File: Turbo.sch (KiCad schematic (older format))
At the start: 25 parts, among them U12 74HCT27, U13 74HCT74, U14 74F86, U15 74F74, U16 74HCT04, U17 74HCT112, U18 74F157, U19 74F157

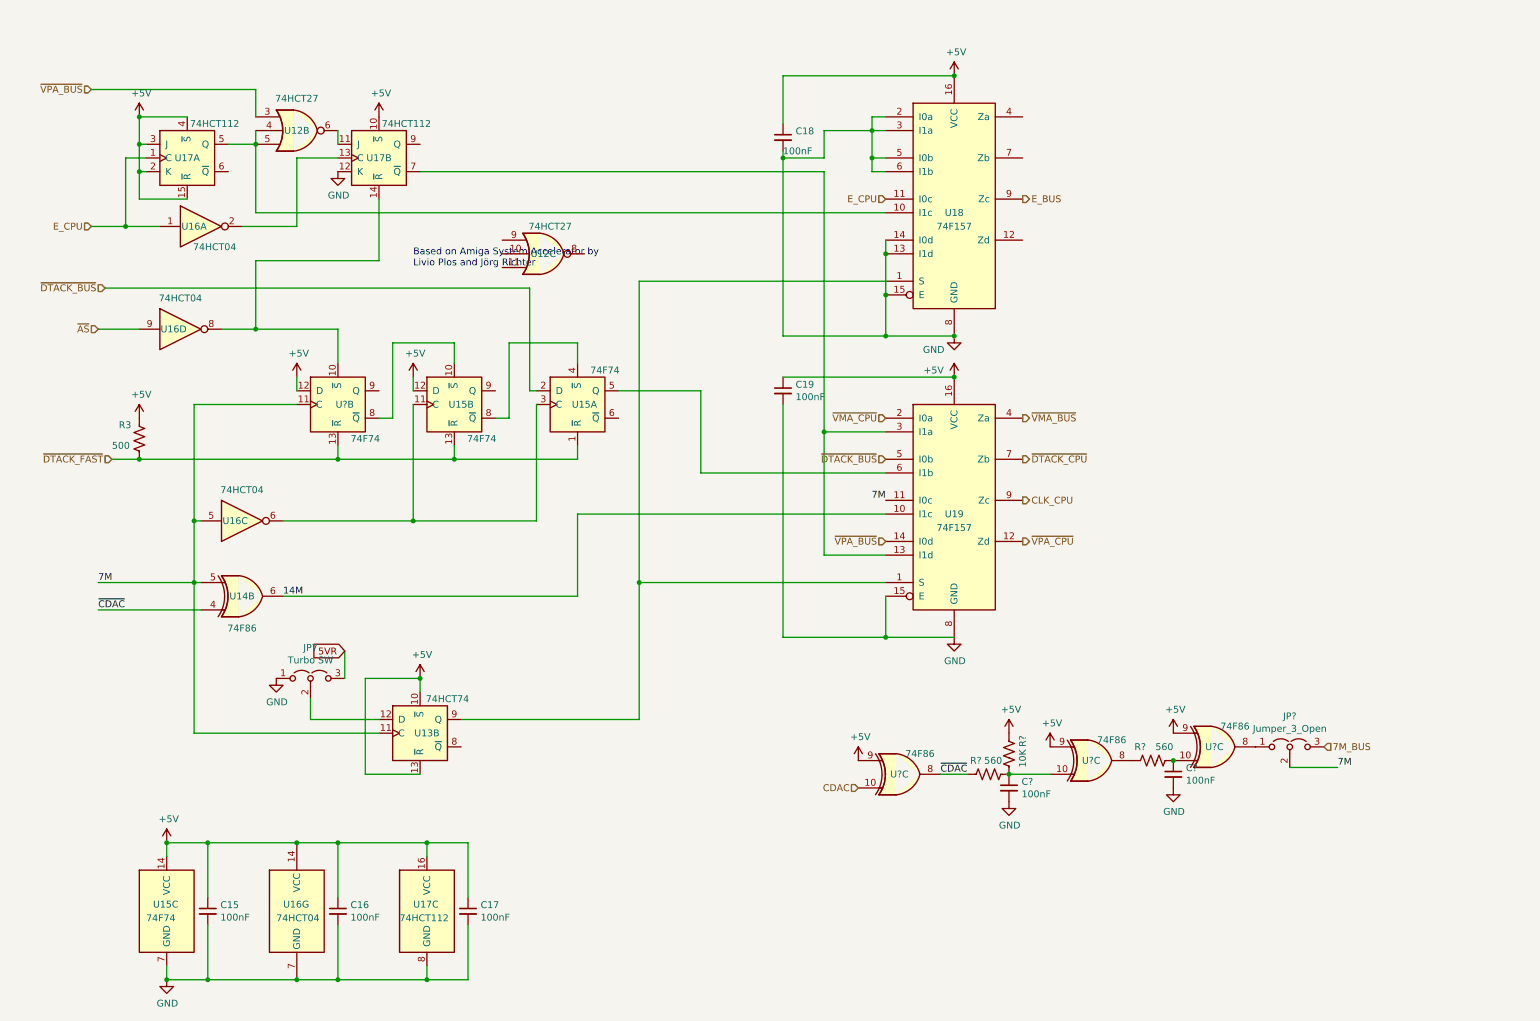
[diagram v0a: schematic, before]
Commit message: AS UDS LDS delay in schematics
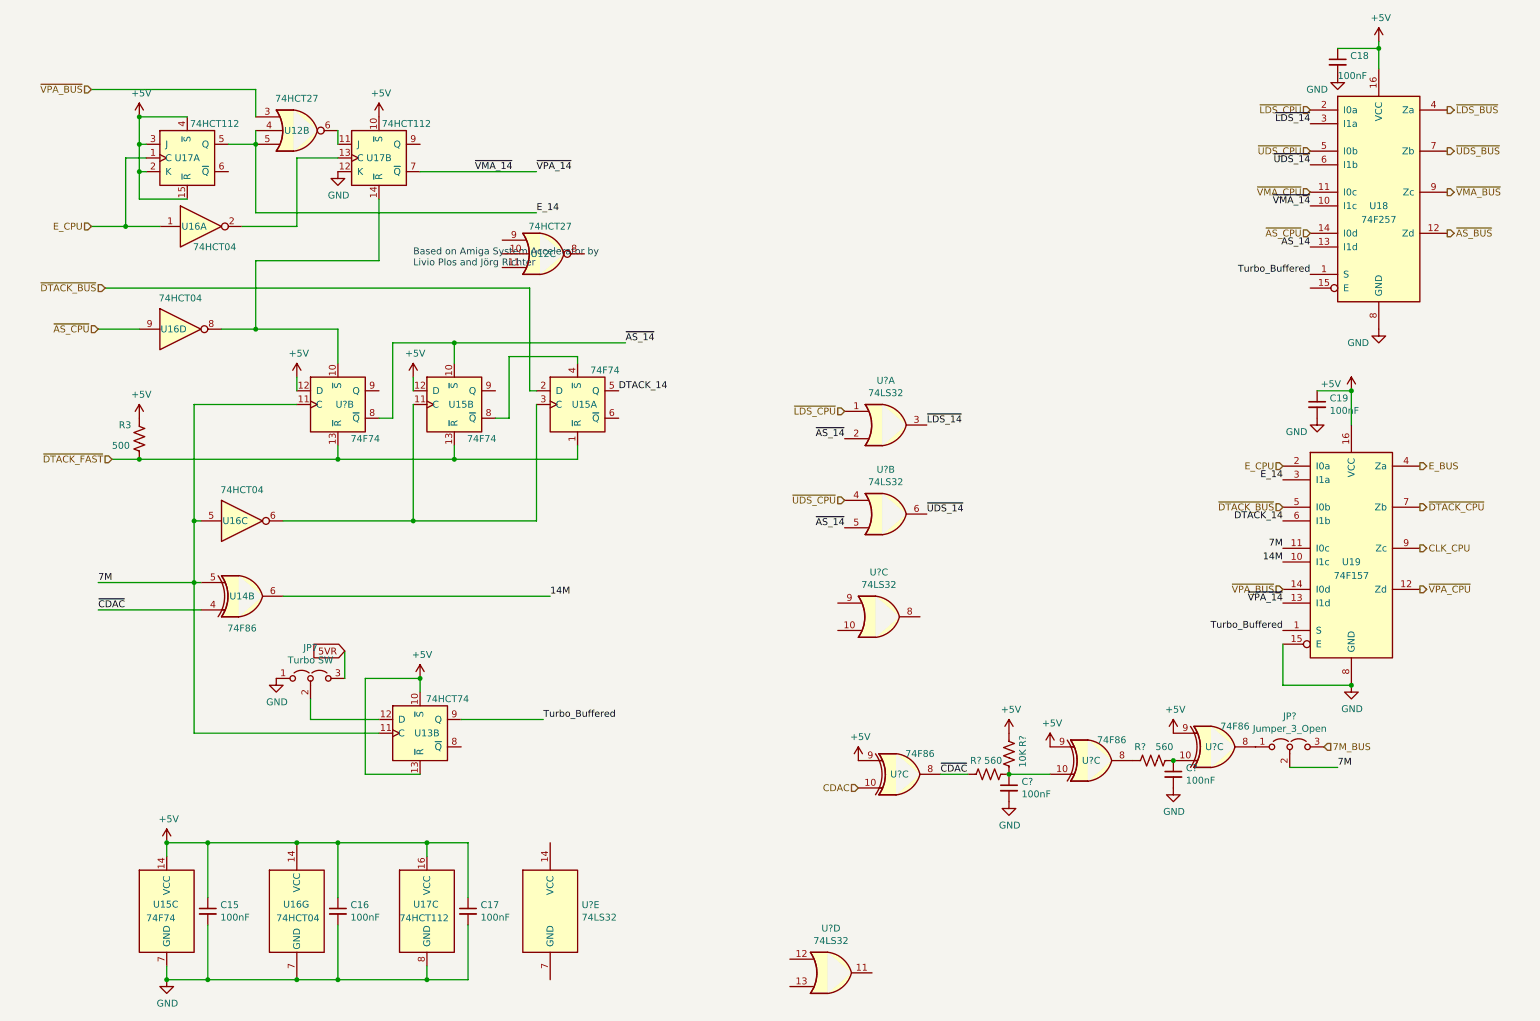
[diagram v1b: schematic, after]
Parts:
- added U? (x5): 74LS32, symbol 74:74LS32
- U18: value 74F157 -> 74F257
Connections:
- net E_BUS: now also U19.4 (Za); no longer U18.9 (Zc)
- net E_CPU: now also U19.2 (I0a); no longer U18.11 (I0c)
- net GND: no longer U18.13 (I1d), U18.14 (I0d), U18.15 (E), U18.2 (I0a), U18.3 (I1a), U18.5 (I0b), U18.6 (I1b)
- net ~VMA_BUS: now also U18.9 (Zc); no longer U19.4 (Za)
- net ~VMA_CPU: now also U18.11 (I0c); no longer U19.2 (I0a)
- net DTACK_14: now reaches U15.5 (Q), U19.6 (I1b)
- net ~AS_14: now reaches U15.10 (~S), U?.8 (~Q)
- net ~AS_14: now also U?.2, U?.5
- net Turbo_Buffered: now reaches U13.9 (Q), U18.1 (S), U19.1 (S)
- net E_14: now reaches U12.4, U12.5, U17.5 (Q)
- net E_14: now also U19.3 (I1a); no longer U18.10 (I1c)
- net ~VMA_14: now reaches U17.7 (~Q), U19.13 (I1d)
- net ~VMA_14: now also U18.10 (I1c); no longer U19.3 (I1a)
- net ~AS_BUS: now reaches U18.12 (Zd)
- net ~LDS_BUS: now reaches U18.4 (Za)
- net ~UDS_BUS: now reaches U18.7 (Zb)
- net ~AS renamed ~AS_CPU
- net ~AS_CPU: now also U18.14 (I0d)
- new net AS_14: U18.13 (I1d)
- new net ~LDS_14: U18.3 (I1a), U?.3
- new net ~LDS_CPU: U18.2 (I0a), U?.1
- new net ~UDS_14: U18.6 (I1b), U?.6
- new net ~UDS_CPU: U18.5 (I0b), U?.4
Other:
- moved on the sheet: C18, C19, U18, U19

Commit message: delay BG
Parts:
- added C?: 100nF, Capacitor_THT:C_Disc_D7.0mm_W2.5mm_P5.00mm, symbol device:C_Small
- added R?: 560, Resistor_THT:R_Axial_DIN0411_L9.9mm_D3.6mm_P12.70mm_Horizontal, symbol device:R_US
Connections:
- net GND: now also C?.2
- net ~AS_BUS: now also R?.1
- net at U?.10: now also C?.1, R?.2
- net ~BG_CPU: now reaches U?.8
- net ~BG_CPU: now also U?.9
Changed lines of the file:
@@
 Text Label 9900 2350 2    50   ~ 0
 Turbo_Buffered
+Text HLabel 6450 4750 0    50   Input ~ 0
+~BG_CPU
+Text HLabel 7050 4850 2    50   Output ~ 0
+~BG_CPU
+Text HLabel 6150 4950 0    50   Input ~ 0
+~AS_BUS
+$Comp
+L device:R_US R?
+U 1 1 61036433
+P 6300 4950
+AR Path="/6068F728/61036433" Ref="R?"  Part="1"
+AR Path="/606B7AE6/61036433" Ref="R?"  Part="1"
+F 0 "R?" V 6400 5000 50  0000 L CNN
+F 1 "560" V 6400 4800 50  0000 L CNN
+F 2 "Resistor_THT:R_Axial_DIN0411_L9.9mm_D3.6mm_P12.70mm_Horizontal" V 6340 4940 50  0001 C CNN
+F 3 "~" H 6300 4950 50  0001 C CNN
+	1    6300 4950
+	0    -1   -1   0
+$EndComp
+$Comp
+L device:C_Small C?
+U 1 1 61036439
+P 6450 5050
+F 0 "C?" H 6542 5096 50  0000 L CNN
+F 1 "100nF" H 6542 5005 50  0000 L CNN
+F 2 "Capacitor_THT:C_Disc_D7.0mm_W2.5mm_P5.00mm" H 6450 5050 50  0001 C CNN
+F 3 "~" H 6450 5050 50  0001 C CNN
+	1    6450 5050
+	1    0    0    -1
+$EndComp
+$Comp
+L OpenAmiga2000CoproAdapter-rescue:GND-power #PWR?
+U 1 1 6103643F
+P 6450 5150
+AR Path="/6103643F" Ref="#PWR?"  Part="1"
+AR Path="/6068F728/6103643F" Ref="#PWR?"  Part="1"
+AR Path="/606B7AE6/6103643F" Ref="#PWR?"  Part="1"
+F 0 "#PWR?" H 6450 4900 50  0001 C CNN
+F 1 "GND" H 6455 4977 50  0000 C CNN
+F 2 "" H 6450 5150 50  0001 C CNN
+F 3 "" H 6450 5150 50  0001 C CNN
+	1    6450 5150
+	1    0    0    -1
+$EndComp
 $EndSCHEMATC

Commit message: pins
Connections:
- net ~BG_CPU: no longer U?.8
- new net ~BG_BUS: U?.8
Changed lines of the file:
@@
 ~BG_CPU
 Text HLabel 7050 4850 2    50   Output ~ 0
-~BG_CPU
+~BG_BUS
 Text HLabel 6150 4950 0    50   Input ~ 0
 ~AS_BUS
